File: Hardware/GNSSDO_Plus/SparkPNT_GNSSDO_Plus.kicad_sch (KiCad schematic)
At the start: 48 parts, among them J7 Qwiic_Vertical, J9 Screw_Cage_3.5mm-10, U1 ESP32-WROVER-IE-N16R8

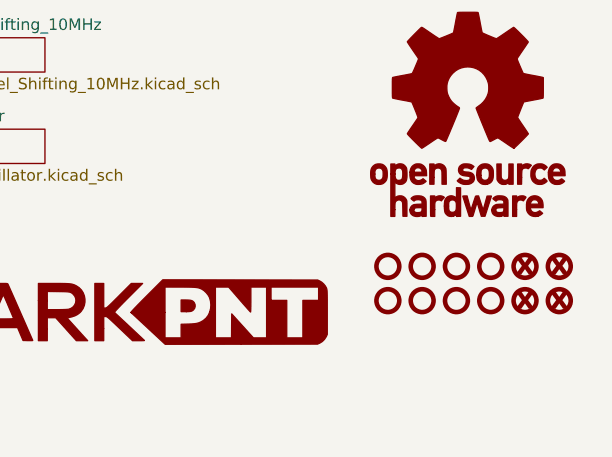
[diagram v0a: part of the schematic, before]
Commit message: GNSSDO Plus: add 3-way splitter
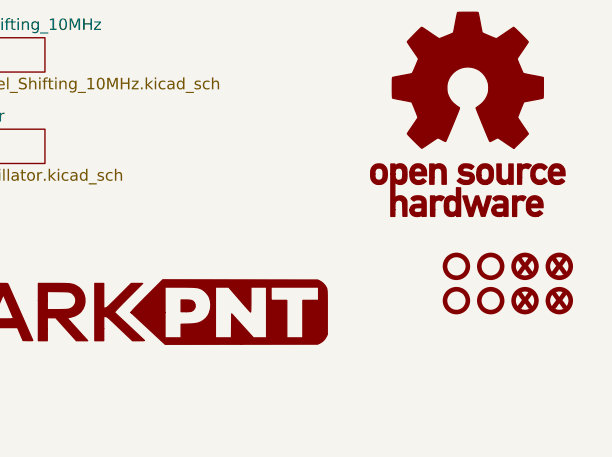
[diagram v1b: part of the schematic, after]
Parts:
- removed ST5, ST6, ST7, ST8: Standoff, SparkFun-Hardware:Standoff, symbol SparkFun-Hardware:Standoff

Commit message: GNSSDO+ WIP
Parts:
- removed R8: 1k, SparkFun-Resistor:R_0603_1608Metric, symbol SparkFun-Resistor:1k_0603
- added JP15: ~, SparkFun-Jumper:Jumper_2_NO, symbol SparkFun-Jumper:SolderJumper_2_Open
- added R8: 2.2k, SparkFun-Resistor:R_0603_1608Metric, symbol SparkFun-Resistor:2.2k_0603
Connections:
- net ESP35/DeviceSense: now also R8.2
- net GND: now also R8.1
- net MCTS2_I: now also J9.4 (Pin_4), JP15.1 (A); no longer J9.3 (Pin_3)
- net MEventB_I: now also J9.3 (Pin_3); no longer J9.2 (Pin_2)
- net MGP1_O: now also J9.2 (Pin_2); no longer J9.1 (Pin_1)
- net MRTS2_O: now also J9.5 (Pin_3); no longer J9.4 (Pin_4)
- net MRX2_I: now also J9.7 (Pin_2); no longer J9.6 (Pin_4)
- net MTX2_O: now also J9.6 (Pin_4); no longer J9.5 (Pin_3)
- net VCCIO: now also JP15.2 (B); no longer J9.7 (Pin_2)
- new net MGP2_O: J9.1 (Pin_1)
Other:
- note added: "Close jumper to use CTS for VCCIO power output"
- moved on the sheet: C53

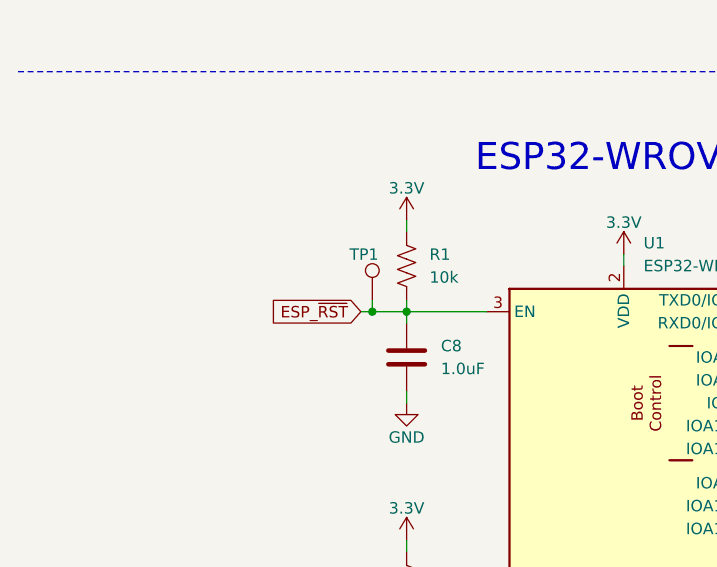
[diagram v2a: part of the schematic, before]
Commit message: GNSSDO+ routed
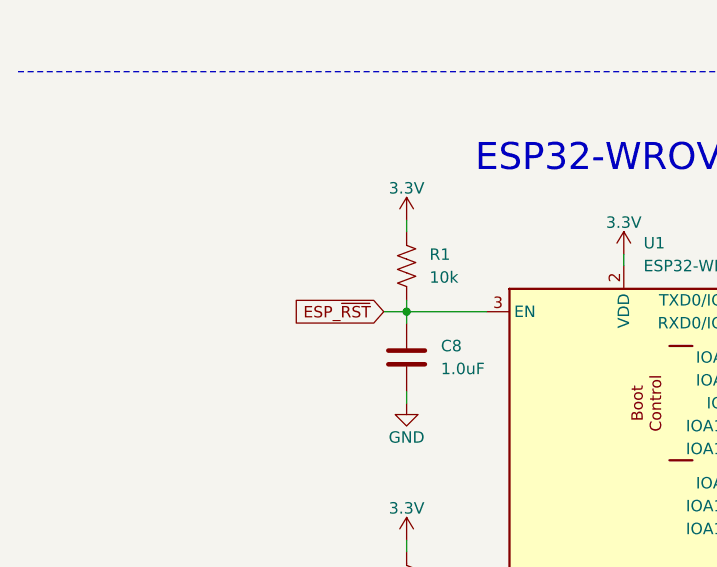
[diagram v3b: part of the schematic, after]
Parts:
- removed TP1: PTH, SparkFun-Connector:1x01, symbol SparkFun-Connector:TestPoint_PTH
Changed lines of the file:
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@@
 	)
 	(junction
-		(at 52.07 116.84)
-		(diameter 0)
-		(color 0 0 0 0)
-	)
-	(junction
 		(at 162.56 45.72)
 		(diameter 0)
@@
 	(wire
 		(pts
-			(xy 52.07 115.57) (xy 52.07 116.84)
-		)
-		(stroke
-			(width 0)
-			(type default)
-		)
-	)
-	(wire
-		(pts
 			(xy 220.98 67.31) (xy 222.25 67.31)
 		)
@@
 	(wire
 		(pts
-			(xy 52.07 116.84) (xy 55.88 116.84)
-		)
-		(stroke
-			(width 0)
-			(type default)
-		)
-	)
-	(wire
-		(pts
 			(xy 162.56 60.96) (xy 162.56 63.5)
 		)
@@
 	(wire
 		(pts
-			(xy 50.8 116.84) (xy 52.07 116.84)
+			(xy 53.34 116.84) (xy 55.88 116.84)
 		)
 		(stroke
@@
 	(global_label "ESP_~{RST}"
 		(shape input)
-		(at 50.8 116.84 180)
+		(at 53.34 116.84 180)
 		(fields_autoplaced yes)
 		(effects
@@
 		)
 		(property "Intersheetrefs" "${INTERSHEET_REFS}"
-			(at 40.7392 116.84 0)
+			(at 43.2792 116.84 0)
 			(effects
 				(font
@@
 					(unit 1)
 				)
-			)
-		)
-	)
-	(symbol
-		(lib_id "SparkFun-Connector:TestPoint_PTH")
-		(at 52.07 115.57 0)
-		(unit 1)
-		(exclude_from_sim no)
-		(in_bom yes)
-		(on_board yes)
-		(dnp no)
-		(property "Reference" "TP1"
-			(at 49.53 110.49 0)
-			(effects
-				(font
-					(size 1.27 1.27)
-				)
-				(justify left)
-			)
-		)
-		(property "Value" "PTH"
-			(at 52.07 119.38 0)
-			(effects
-				(font
-					(size 1.27 1.27)
-				)
-				(hide yes)
-			)
-		)
-		(property "Footprint" "SparkFun-Connector:1x01"
-			(at 50.8 121.92 0)
-			(effects
-				(font
-					(size 1.27 1.27)
-				)
-				(hide yes)
-			)
-		)
-		(property "Datasheet" "~"
-			(at 52.07 123.19 0)
-			(effects
-				(font
-					(size 1.27 1.27)
-				)
-				(hide yes)
-			)
-		)
-		(property "Description" "Test Point"
-			(at 52.07 115.57 0)
-			(effects
-				(font
-					(size 1.27 1.27)
-				)
-				(hide yes)
-			)
-		)
-		(pin "1"
-		)
-		(instances
-			(project "SparkFun_RTK_mosaic-T"
-				(path "/e3dd3ae4-244d-4cba-9cca-5d2abf83f29a"
-					(reference "TP1")
-					(unit 1)
-				)

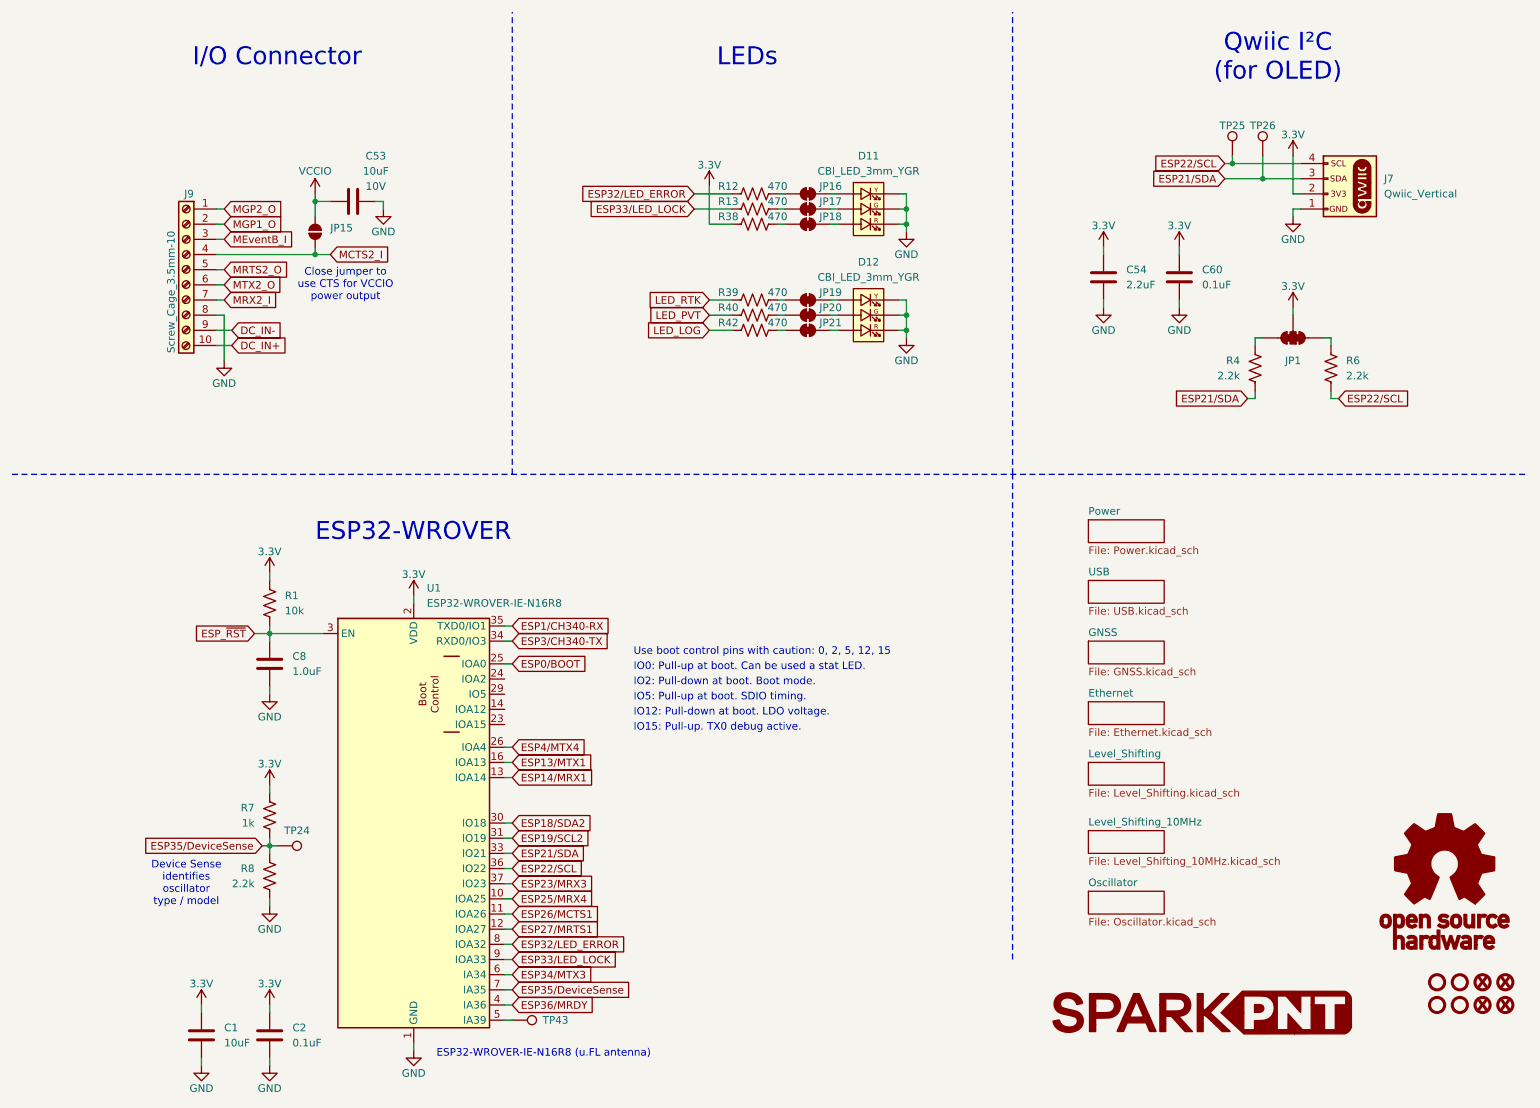
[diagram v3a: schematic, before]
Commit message: GNSSDO+ : update symbols and footprints
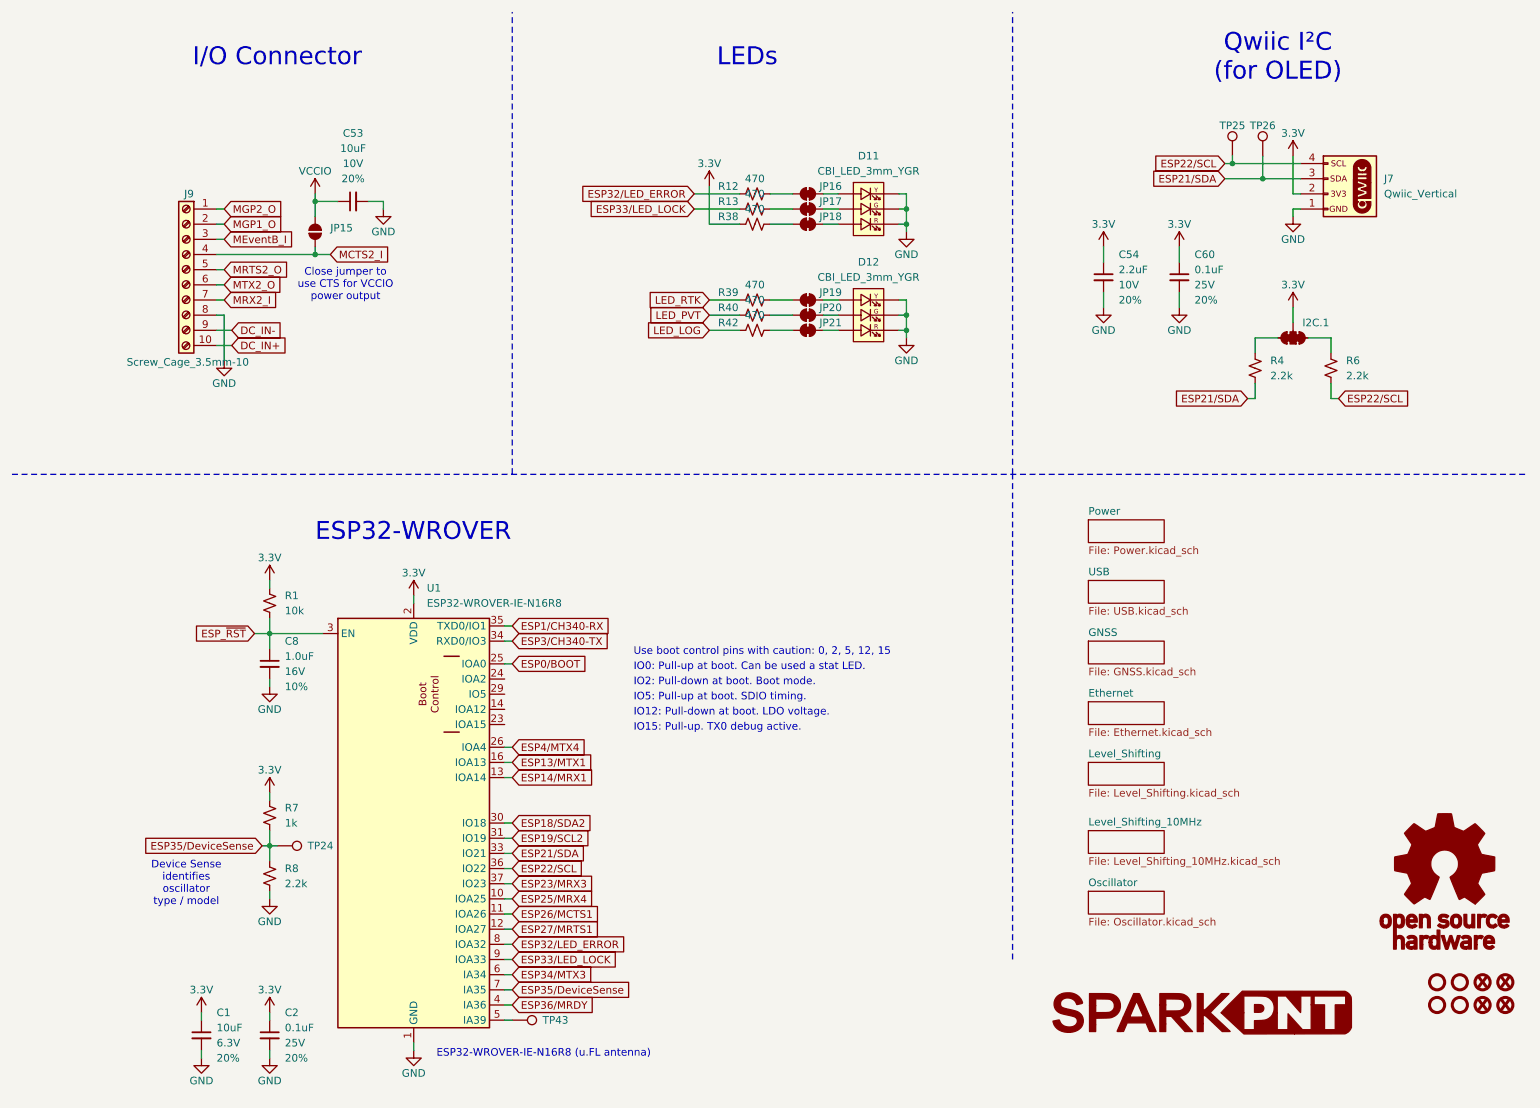
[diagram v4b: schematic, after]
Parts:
- renumbered JP1 to I2C.1
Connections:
- net 3.3V: now also R1.2, R38.1, R7.2; no longer R1.1, R38.2, R7.1
- net ESP21/SDA: now also R4.2; no longer R4.1
- net ESP22/SCL: now also R6.2; no longer R6.1
- net ESP32/LED_ERROR: now also R12.1; no longer R12.2
- net ESP33/LED_LOCK: now also R13.1; no longer R13.2
- net ESP35/DeviceSense: now also R7.1, R8.1; no longer R7.2, R8.2
- net ESP_~{RST}: now also R1.1; no longer R1.2
- net GND: now also R8.2; no longer R8.1
- net LED_LOG: now also R42.1; no longer R42.2
- net LED_PVT: now also R40.1; no longer R40.2
- net LED_RTK: now also R39.1; no longer R39.2
- net at JP18.1 (A): now also R38.2; no longer R38.1
- net at I2C.1.3 (C): now also R4.1; no longer R4.2
- net at JP20.1 (A): now also R40.2; no longer R40.1
- net at I2C.1.1 (A): now also R6.1; no longer R6.2
- net at JP19.1 (A): now also R39.2; no longer R39.1
- net at JP16.1 (A): now also R12.2; no longer R12.1
- net at JP17.1 (A): now also R13.2; no longer R13.1
- net at JP21.1 (A): now also R42.2; no longer R42.1
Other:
- moved on the sheet: I2C.1

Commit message: GNSSDO Plus - ready for review
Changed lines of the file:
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@@
 		)
 		(property "Value" "470"
-			(at 137.16 45.72 0)
+			(at 140.97 46.99 0)
 			(effects
 				(font
@@
 		)
 		(property "Value" "470"
-			(at 137.16 40.64 0)
+			(at 140.97 41.91 0)
 			(effects
 				(font
@@
 		)
 		(property "Value" "470"
-			(at 137.16 60.96 0)
+			(at 140.97 62.23 0)
 			(effects
 				(font
@@
 		)
 		(property "Value" "470"
-			(at 137.16 43.18 0)
+			(at 140.97 44.45 0)
 			(effects
 				(font
@@
 		)
 		(property "Value" "470"
-			(at 137.16 63.5 0)
+			(at 140.97 64.77 0)
 			(effects
 				(font
@@
 		)
 		(property "Value" "470"
-			(at 137.16 58.42 0)
+			(at 140.97 59.69 0)
 			(effects
 				(font

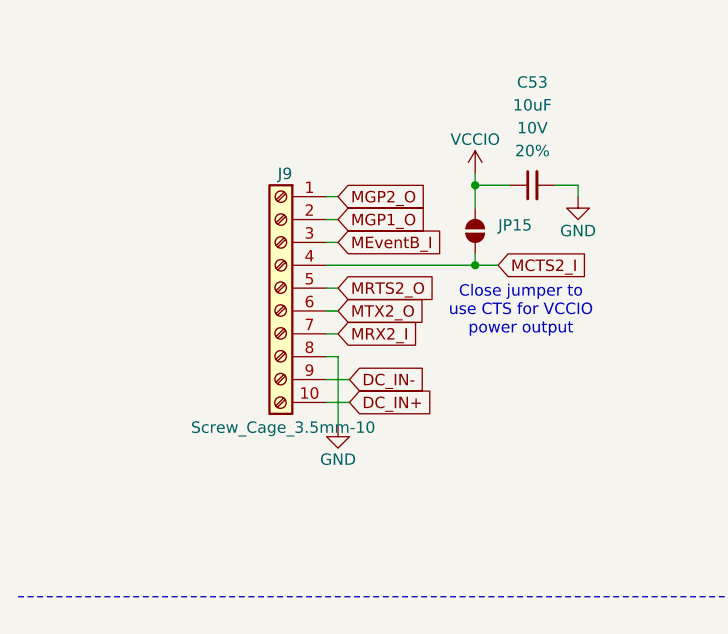
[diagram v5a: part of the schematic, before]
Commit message: GNSSDO+ PCB ready for protos
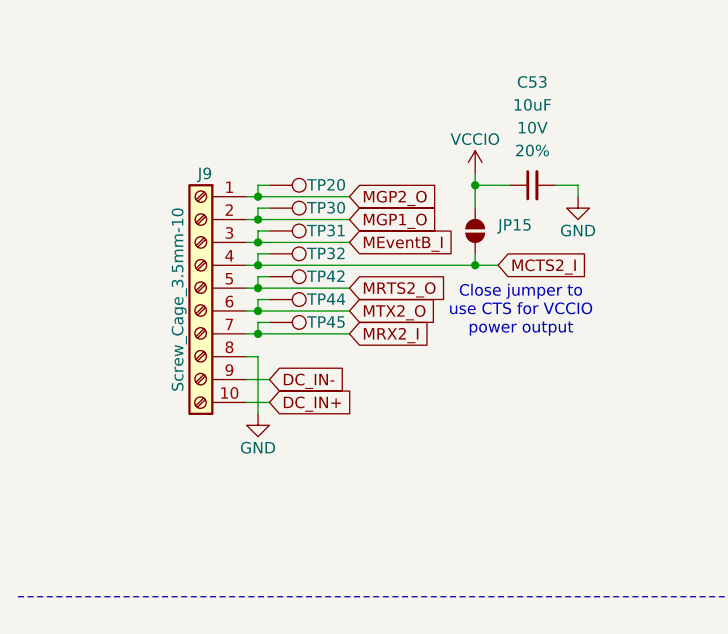
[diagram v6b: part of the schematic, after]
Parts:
- added TP20, TP30, TP31, TP32, TP42, TP44, TP45: 1.25mm, SparkFun-Connector:TestPoint-1.25mm, symbol SparkFun-Connector:TestPoint_1.25mm
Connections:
- net MCTS2_I: now also TP32.1
- net MEventB_I: now also TP31.1
- net MGP1_O: now also TP30.1
- net MGP2_O: now also TP20.1
- net MRTS2_O: now also TP42.1
- net MRX2_I: now also TP45.1
- net MTX2_O: now also TP44.1
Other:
- moved on the sheet: J9
